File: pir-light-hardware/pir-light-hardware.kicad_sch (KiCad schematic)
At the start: 43 parts, among them J1 ZH1.5-3, J2 ZH1.5-3, Q1 DTC114EUA-TP, Q2 AON7240, Q3 DTA114EUAHE3-TP, Q7 DTA114EUAHE3-TP, U1 AS312, U2 M74VHC1GT08DFT2G, U3 LMV331IDCKR, U4 LMV331IDCKR

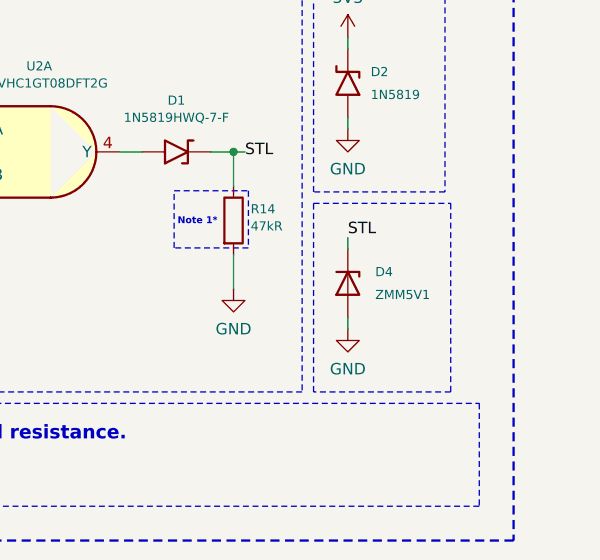
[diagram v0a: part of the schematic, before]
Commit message: chore: mark general PCB dimensions
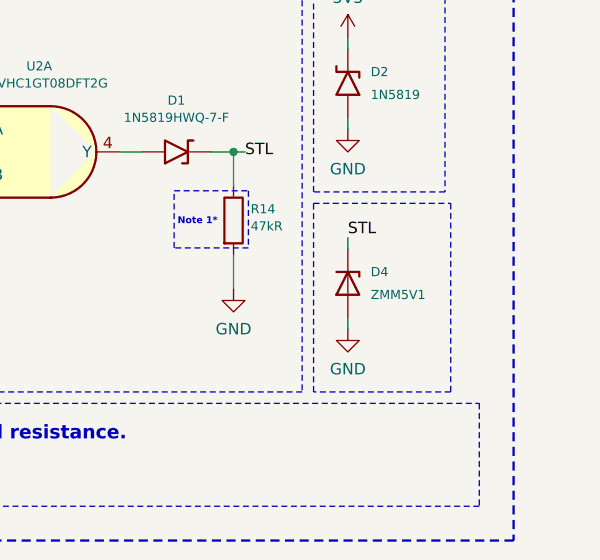
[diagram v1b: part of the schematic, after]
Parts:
- D2: footprint Diode_SMD:D_SOD-123F -> REST:D_SOD-123F
- D4: footprint Diode_SMD:D_MiniMELF -> REST:D_MiniMELF
- F1: footprint (none) -> REST:R_1206_3216Metric
- U1: footprint (none) -> AS312:AS312-NEW
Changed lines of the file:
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@@
 			)
 		)
-		(property "Footprint" ""
+		(property "Footprint" "REST:R_1206_3216Metric"
 			(at 44.577 54.61 90)
 			(hide yes)
@@
 			)
 		)
-		(property "Footprint" "Diode_SMD:D_SOD-123F"
+		(property "Footprint" "REST:D_SOD-123F"
 			(at 161.62 104.775 0)
 			(hide yes)
@@
 			)
 		)
-		(property "Footprint" ""
+		(property "Footprint" "AS312:AS312-NEW"
 			(at 146.05 52.705 0)
 			(hide yes)
@@
 		(fields_autoplaced yes)
 		(property "Reference" "D4"
-			(at 258.318 113.0299 90)
+			(at 257.81 113.0299 90)
 			(show_name no)
 			(do_not_autoplace no)
@@
 		)
 		(property "Value" "ZMM5V1"
-			(at 258.318 115.5699 90)
+			(at 257.81 115.5699 90)
 			(show_name no)
 			(do_not_autoplace no)
@@
 			)
 		)
-		(property "Footprint" "Diode_SMD:D_MiniMELF"
+		(property "Footprint" "REST:D_MiniMELF"
 			(at 250.825 114.3 0)
 			(hide yes)

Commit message: chore: add top pcb layout
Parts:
- C7: renamed from C12; footprint REST:CP_Elec_4x5.4 -> REST:CP_EIA-3528-12_Kemet-T
- renumbered C9 to C10, C10 to C11, C11 to C12, C5 to C4, C6 to C5, C7 to C6, C4 to C8, C8 to C9, D2 to D1, D1 to D2, D4 to D3, Q3 to Q1, Q7 to Q3, Q1 to Q4, R12 to R10, R14 to R11, R15 to R12, R16 to R13, R9 to R8, R10 to R9
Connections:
- net STL: now also J1.2, J2.2; no longer J1.3, J2.1
- net VIN: now also J1.3, J2.1; no longer J1.2, J2.2
